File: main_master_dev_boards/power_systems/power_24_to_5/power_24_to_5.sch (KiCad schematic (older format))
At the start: 31 parts, among them J1 Switch_in, J2 24_in, J3 GND_in, J4 PGoodMain_out, J5 ref_out, J6 5_out, J7 GND_out, J8 3v3_out, J9 PGoodBackup_out, U1 LMR16030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

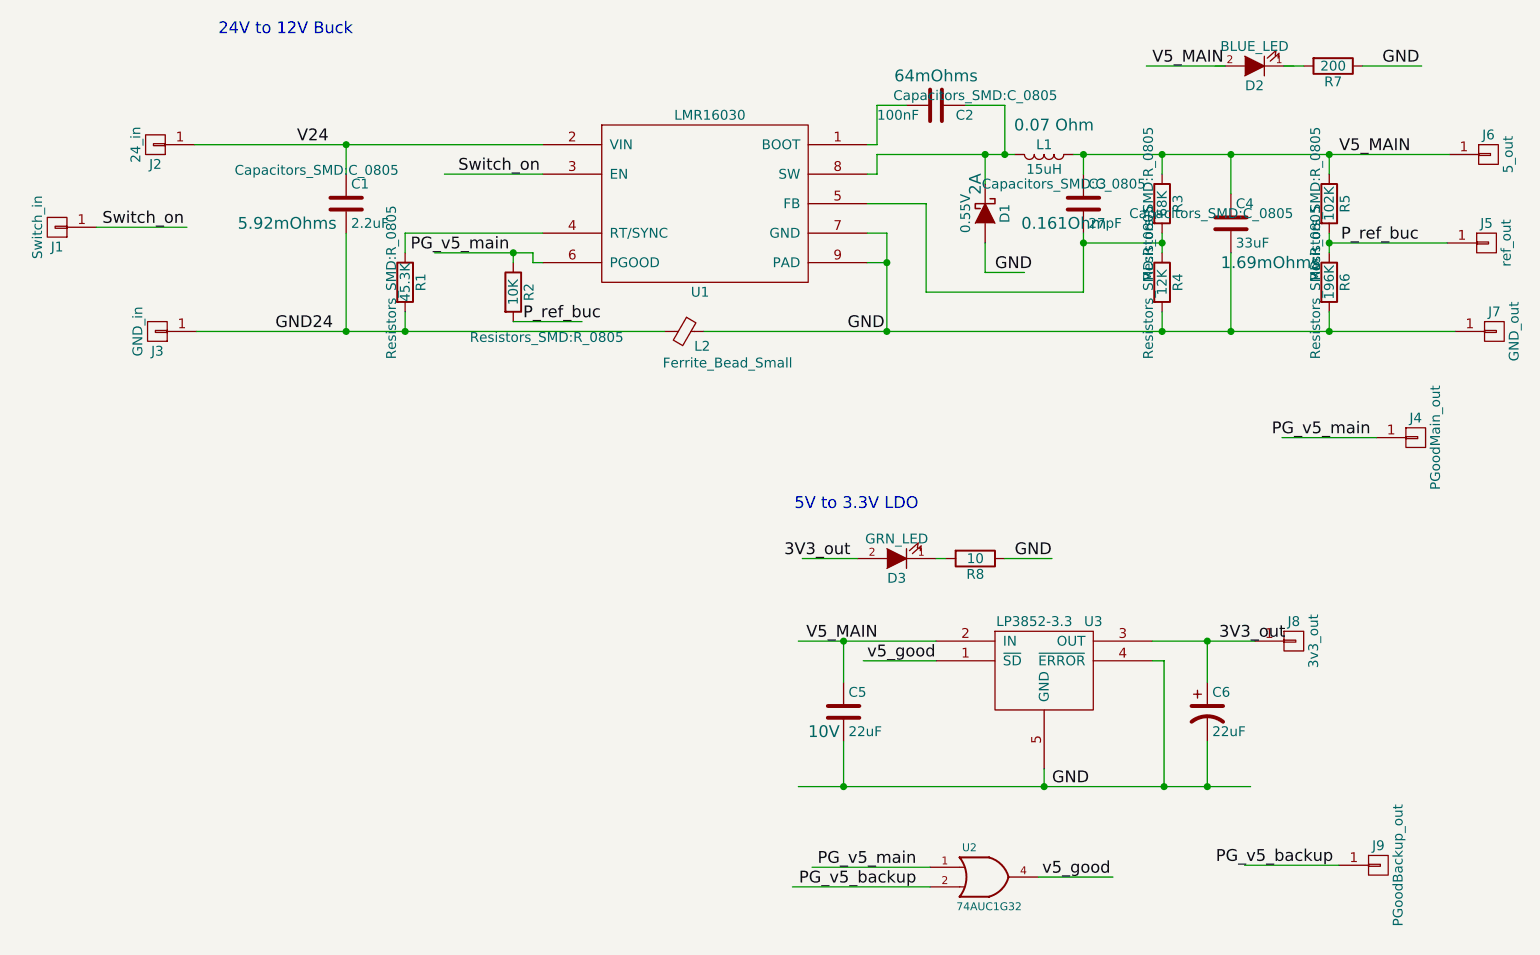
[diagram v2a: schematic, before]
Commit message: Redesigned 24 to 5 dev board
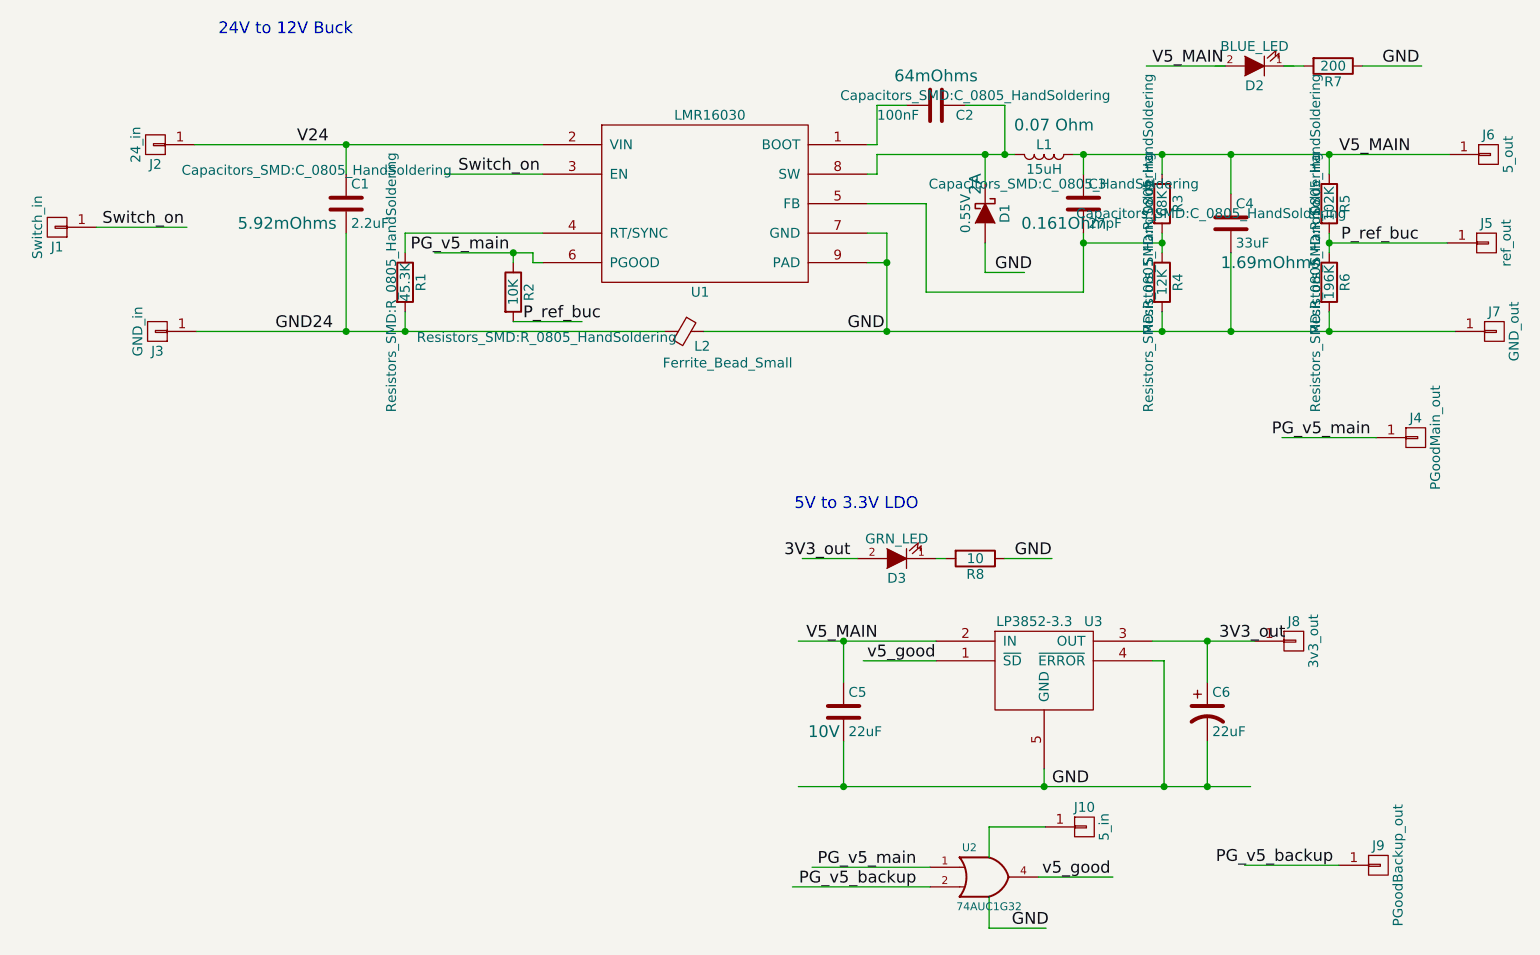
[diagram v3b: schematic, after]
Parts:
- added J10: 5_in, pinheaders:pinhead-01x01_3x1, symbol CONN_01X01
- C1, C2, C3, C4: footprint Capacitors_SMD:C_0805 -> Capacitors_SMD:C_0805_HandSoldering
- C5, C6: footprint Capacitors_SMD:C_0603 -> Capacitors_SMD:C_0805_HandSoldering
- J1, J2, J4, J5, J6, J8, J9: footprint Pin_Headers:Pin_Header_Straight_1x01_Pitch2.54mm -> pinheaders:pinhead-01x01_3x1
- J3, J7: footprint Pin_Headers:Pin_Header_Straight_1x01_Pitch2.54mm -> pinheaders:pinhead-01x01_3x1_square
- L2: footprint Capacitors_SMD:C_0603_HandSoldering -> Capacitors_SMD:C_0805_HandSoldering
- R1, R2, R3, R4, R5, R6, R7: footprint Resistors_SMD:R_0805 -> Resistors_SMD:R_0805_HandSoldering
- R8: footprint Resistors_SMD:R_0603 -> Resistors_SMD:R_0805_HandSoldering
- U1: footprint HSOIC-8:HSOIC-8-1EP_Pitch1.27mm -> HSOIC-8:HSOIC-8-1EP_Pitch1.27mm_noVias
- U2: footprint SO-70:SO-70 -> TO_SOT_Packages_SMD:SOT-23-5_HandSoldering
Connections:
- wire segments 67 -> 71
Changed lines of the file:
@@
 LIBS:contrib
 LIBS:valves
+LIBS:antenna
+LIBS:AS1360
+LIBS:conn_2x45
+LIBS:conn_2x50
+LIBS:conn_open_q_x2
+LIBS:esd7c5
+LIBS:FDS4935A
+LIBS:FPF1203LUCX
+LIBS:lan9512
+LIBS:LMR16020
+LIBS:LP3852-3.3
+LIBS:LTC2955-1
+LIBS:MIC2026
+LIBS:Si1077X
+LIBS:Si1900DL
+LIBS:SN74LV1T125
+LIBS:SN74LV4T125
+LIBS:TDP6E001RSER
+LIBS:tps82084sil
+LIBS:TPS754
+LIBS:TPS61089
+LIBS:TPS61232DRC
+LIBS:TPS832130SIL
+LIBS:0s102011ma1qn1
+LIBS:74LVC1G17
+LIBS:74V1T126
+LIBS:acs711klctr-12ab-t
+LIBS:AD7192
+LIBS:AD7193
+LIBS:am-hrr30-xxx
+LIBS:aon7528
+LIBS:AP7363
+LIBS:AS1359
+LIBS:csd16323q3
+LIBS:dmn2004dmk
+LIBS:dp_devices
+LIBS:DSPIC33E128MC506
+LIBS:fds6898az
+LIBS:ina197
+LIBS:irf7329pbf
+LIBS:ld1117
+LIBS:lm3478
+LIBS:lm3481
+LIBS:lt1910
+LIBS:ltc1871
+LIBS:ltc1982
+LIBS:MAG3110
+LIBS:mcp1700
+LIBS:mcp73831
+LIBS:mcsmt-g5030a1-3712
+LIBS:microchip_can
+LIBS:microclasp_hdrx2
+LIBS:microclasp_hdrx3
+LIBS:MPU-6000_MPU-6050
+LIBS:MPU-9150
+LIBS:nrf24l01+
+LIBS:pds1040l
+LIBS:pic12f1571
+LIBS:pinhead
+LIBS:psmn013-80ys
+LIBS:RESISTOR_ARRAY
+LIBS:rf803d
+LIBS:RGB_LED
+LIBS:Si1970DH
+LIBS:sn65hvd232
+LIBS:ssc54
+LIBS:sw_push_4
+LIBS:tc74
+LIBS:tps54540
+LIBS:TPS2113A
+LIBS:vs-mbrb1635pbf
+LIBS:xal5050-562meb
+LIBS:xal6030-182mec
+LIBS:ld29150dt50r
+LIBS:ncp59151ds50r4g
+LIBS:pinhd-2x23
 LIBS:main_master_board-cache
 LIBS:power_24_to_5-cache
@@
 F 0 "C3" H 6075 2700 50  0000 L CNN
 F 1 "27pF" H 6075 2500 50  0000 L CNN
-F 2 "Capacitors_SMD:C_0805" H 5950 2700 50  0000 C CNN
+F 2 "Capacitors_SMD:C_0805_HandSoldering" H 5950 2700 50  0000 C CNN
 F 3 "" H 6050 2600 50  0000 C CNN
 F 4 "0.161Ohm" H 5950 2500 60  0000 C CNN "Resistance"
@@
 F 0 "C1" H 2325 2700 50  0000 L CNN
 F 1 "2.2uF" H 2325 2500 50  0000 L CNN
-F 2 "Capacitors_SMD:C_0805" H 2150 2770 50  0000 C CNN
+F 2 "Capacitors_SMD:C_0805_HandSoldering" H 2150 2770 50  0000 C CNN
 F 3 "" H 2300 2600 50  0001 C CNN
 F 4 "5.92mOhms" H 2000 2500 60  0000 C CNN "Resistance"
@@
 F 0 "R1" V 2680 3000 50  0000 C CNN
 F 1 "45.3K" V 2600 3000 50  0000 C CNN
-F 2 "Resistors_SMD:R_0805" V 2530 3000 50  0000 C CNN
+F 2 "Resistors_SMD:R_0805_HandSoldering" V 2530 3000 50  0000 C CNN
 F 3 "" H 2600 3000 50  0000 C CNN
 F 4 "d" V 2600 3000 60  0001 C CNN "Field4"
@@
 F 0 "C2" V 5350 2200 50  0000 L CNN
 F 1 "100nF" V 5350 1800 50  0000 L CNN
-F 2 "Capacitors_SMD:C_0805" V 5250 2300 50  0000 C CNN
+F 2 "Capacitors_SMD:C_0805_HandSoldering" V 5250 2300 50  0000 C CNN
 F 3 "https://product.tdk.com/info/en/catalog/datasheets/mlcc%5Fcommercial%5Fgeneral%5Fen.pdf" H 5300 2100 50  0001 C CNN
 F 4 "64mOhms" V 5150 2100 60  0000 C CNN "Resistance"
@@
 F 0 "R3" V 6530 2600 50  0000 C CNN
 F 1 "68K" V 6450 2600 50  0000 C CNN
-F 2 "Resistors_SMD:R_0805" V 6380 2600 50  0000 C CNN
+F 2 "Resistors_SMD:R_0805_HandSoldering" V 6380 2600 50  0000 C CNN
 F 3 "" H 6450 2600 50  0000 C CNN
 F 4 "d" V 6450 2600 60  0001 C CNN "Field4"
@@
 F 0 "R4" V 6530 3000 50  0000 C CNN
 F 1 "12K" V 6450 3000 50  0000 C CNN
-F 2 "Resistors_SMD:R_0805" V 6380 3000 50  0000 C CNN
+F 2 "Resistors_SMD:R_0805_HandSoldering" V 6380 3000 50  0000 C CNN
 F 3 "" H 6450 3000 50  0000 C CNN
 F 4 "d" V 6450 3000 60  0001 C CNN "Field4"
@@
 F 0 "C4" H 6825 2800 50  0000 L CNN
 F 1 "33uF" H 6825 2600 50  0000 L CNN
-F 2 "Capacitors_SMD:C_0805" H 6700 2750 50  0000 C CNN
+F 2 "Capacitors_SMD:C_0805_HandSoldering" H 6700 2750 50  0000 C CNN
 F 3 "" H 6800 2700 50  0000 C CNN
 F 4 "1.69mOhms" H 7000 2500 60  0000 C CNN "Resistance"
@@
 F 0 "R2" V 3230 3050 50  0000 C CNN
 F 1 "10K" V 3150 3050 50  0000 C CNN
-F 2 "Resistors_SMD:R_0805" H 3320 2820 50  0000 C CNN
+F 2 "Resistors_SMD:R_0805_HandSoldering" H 3320 2820 50  0000 C CNN
 F 3 "" H 3150 3050 50  0000 C CNN
 	1    3150 3050
@@
 F 0 "R7" V 7400 1900 50  0000 C CNN
 F 1 "200" V 7320 1900 50  0000 C CNN
-F 2 "Resistors_SMD:R_0805" V 7250 1900 50  0001 C CNN
+F 2 "Resistors_SMD:R_0805_HandSoldering" V 7250 1900 50  0001 C CNN
 F 3 "" H 7320 1900 50  0000 C CNN
 	1    7320 1900
@@
 F 0 "U1" H 4100 2150 50  0000 C CNN
 F 1 "LMR16030" H 4150 3050 50  0000 C CNN
-F 2 "HSOIC-8:HSOIC-8-1EP_Pitch1.27mm" H 3750 2150 50  0001 C CNN
+F 2 "HSOIC-8:HSOIC-8-1EP_Pitch1.27mm_noVias" H 3750 2150 50  0001 C CNN
 F 3 "http://www.digikey.com/product-detail/en/LMR16030PDDA/296-44513-5-ND/" H 4550 2150 50  0001 C CNN
 	1    4150 2600
@@
 F 0 "R5" V 7380 2600 50  0000 C CNN
 F 1 "102K" V 7300 2600 50  0000 C CNN
-F 2 "Resistors_SMD:R_0805" V 7230 2600 50  0000 C CNN
+F 2 "Resistors_SMD:R_0805_HandSoldering" V 7230 2600 50  0000 C CNN
 F 3 "" H 7300 2600 50  0000 C CNN
 	1    7300 2600
@@
 F 0 "R6" V 7380 3000 50  0000 C CNN
 F 1 "196K" V 7300 3000 50  0000 C CNN
-F 2 "Resistors_SMD:R_0805" V 7230 3000 50  0000 C CNN
+F 2 "Resistors_SMD:R_0805_HandSoldering" V 7230 3000 50  0000 C CNN
 F 3 "" H 7300 3000 50  0000 C CNN
 	1    7300 3000
@@
 F 0 "J2" H 1330 2400 50  0000 C CNN
 F 1 "24_in" V 1430 2300 50  0000 C CNN
-F 2 "Pin_Headers:Pin_Header_Straight_1x01_Pitch2.54mm" H 1330 2300 50  0001 C CNN
+F 2 "pinheaders:pinhead-01x01_3x1" H 1330 2300 50  0001 C CNN
 F 3 "" H 1330 2300 50  0001 C CNN
 	1    1330 2300
@@
 F 0 "J3" H 1340 3350 50  0000 C CNN
 F 1 "GND_in" V 1440 3250 50  0000 C CNN
-F 2 "Pin_Headers:Pin_Header_Straight_1x01_Pitch2.54mm" H 1340 3250 50  0001 C CNN
+F 2 "pinheaders:pinhead-01x01_3x1_square" H 1340 3250 50  0001 C CNN
 F 3 "" H 1340 3250 50  0001 C CNN
 	1    1340 3250
@@
 F 0 "J4" H 7740 3890 50  0000 C CNN
 F 1 "PGoodMain_out" V 7840 3790 50  0000 C CNN
-F 2 "Pin_Headers:Pin_Header_Straight_1x01_Pitch2.54mm" H 7740 3790 50  0001 C CNN
+F 2 "pinheaders:pinhead-01x01_3x1" H 7740 3790 50  0001 C CNN
 F 3 "" H 7740 3790 50  0001 C CNN
 	1    7740 3790
@@
 F 0 "J6" H 8110 2450 50  0000 C CNN
 F 1 "5_out" V 8210 2350 50  0000 C CNN
-F 2 "Pin_Headers:Pin_Header_Straight_1x01_Pitch2.54mm" H 8110 2350 50  0001 C CNN
+F 2 "pinheaders:pinhead-01x01_3x1" H 8110 2350 50  0001 C CNN
 F 3 "" H 8110 2350 50  0001 C CNN
 	1    8110 2350
@@
 F 0 "J7" H 8140 3350 50  0000 C CNN
 F 1 "GND_out" V 8240 3250 50  0000 C CNN
-F 2 "Pin_Headers:Pin_Header_Straight_1x01_Pitch2.54mm" H 8140 3250 50  0001 C CNN
+F 2 "pinheaders:pinhead-01x01_3x1_square" H 8140 3250 50  0001 C CNN
 F 3 "" H 8140 3250 50  0001 C CNN
 	1    8140 3250
@@
 F 0 "J5" H 8100 2900 50  0000 C CNN
 F 1 "ref_out" V 8200 2800 50  0000 C CNN
-F 2 "Pin_Headers:Pin_Header_Straight_1x01_Pitch2.54mm" H 8100 2800 50  0001 C CNN
+F 2 "pinheaders:pinhead-01x01_3x1" H 8100 2800 50  0001 C CNN
 F 3 "" H 8100 2800 50  0001 C CNN
 	1    8100 2800
@@
 F 0 "J1" H 830 2820 50  0000 C CNN
 F 1 "Switch_in" V 930 2720 50  0000 C CNN
-F 2 "Pin_Headers:Pin_Header_Straight_1x01_Pitch2.54mm" H 830 2720 50  0001 C CNN
+F 2 "pinheaders:pinhead-01x01_3x1" H 830 2720 50  0001 C CNN
 F 3 "" H 830 2720 50  0001 C CNN
 	1    830  2720
@@
 F 0 "L2" V 4095 3300 50  0000 L CNN
 F 1 "Ferrite_Bead_Small" V 4180 3140 50  0000 L CNN
-F 2 "Capacitors_SMD:C_0603_HandSoldering" V 3950 3250 50  0001 C CNN
+F 2 "Capacitors_SMD:C_0805_HandSoldering" V 3950 3250 50  0001 C CNN
 F 3 "https://www.digikey.com/product-detail/en/BLM18PG121SN1D/490-1037-1-ND/" H 4020 3250 50  0001 C CNN
 	1    4020 3250
@@
 F 0 "R8" V 5580 4405 50  0000 C CNN
 F 1 "10" V 5500 4405 50  0000 C CNN
-F 2 "Resistors_SMD:R_0603" V 5430 4405 50  0001 C CNN
+F 2 "Resistors_SMD:R_0805_HandSoldering" V 5430 4405 50  0001 C CNN
 F 3 "" H 5500 4405 50  0000 C CNN
 	1    5500 4405
@@
 F 0 "C5" H 4855 5285 50  0000 L CNN
 F 1 "22uF" H 4855 5085 50  0000 L CNN
-F 2 "Capacitors_SMD:C_0603" H 4868 5035 50  0001 C CNN
+F 2 "Capacitors_SMD:C_0805_HandSoldering" H 4868 5035 50  0001 C CNN
 F 3 "" H 4830 5185 50  0000 C CNN
 F 4 "10V" H 4730 5085 60  0000 C CNN "Voltage"
@@
 F 0 "C6" H 6705 5285 50  0000 L CNN
 F 1 "22uF" H 6705 5085 50  0000 L CNN
-F 2 "Capacitors_SMD:C_0603" H 6680 5185 50  0001 C CNN
+F 2 "Capacitors_SMD:C_0805_HandSoldering" H 6680 5185 50  0001 C CNN
 F 3 "" H 6680 5185 50  0000 C CNN
 	1    6680 5185
@@
 F 0 "U2" H 5470 6175 40  0000 C CNN
 F 1 "74AUC1G32" H 5570 5875 40  0000 C CNN
-F 2 "SO-70:SO-70" H 5570 6025 60  0001 C CNN
+F 2 "TO_SOT_Packages_SMD:SOT-23-5_HandSoldering" H 5570 6025 60  0001 C CNN
 F 3 "https://octopart.com/sn74auc1g32dckr-texas+instruments-464483" H 5570 6025 60  0001 C CNN
 	1    5570 6025
@@
 F 0 "J9" H 7550 6065 50  0000 C CNN
 F 1 "PGoodBackup_out" V 7650 5965 50  0000 C CNN
-F 2 "Pin_Headers:Pin_Header_Straight_1x01_Pitch2.54mm" H 7550 5965 50  0001 C CNN
+F 2 "pinheaders:pinhead-01x01_3x1" H 7550 5965 50  0001 C CNN
 F 3 "" H 7550 5965 50  0001 C CNN
 	1    7550 5965
@@
 F 0 "J8" H 7120 4925 50  0000 C CNN
 F 1 "3v3_out" V 7220 4825 50  0000 C CNN
-F 2 "Pin_Headers:Pin_Header_Straight_1x01_Pitch2.54mm" H 7120 4825 50  0001 C CNN
+F 2 "pinheaders:pinhead-01x01_3x1" H 7120 4825 50  0001 C CNN
 F 3 "" H 7120 4825 50  0001 C CNN
 	1    7120 4825
@@
 Text Label 4865 4405 2    60   ~ 0
 3V3_out
+Wire Wire Line
+	5570 5925 5570 5770
+Wire Wire Line
+	5570 5770 5855 5770
+Wire Wire Line
+	5570 6125 5570 6285
+Wire Wire Line
+	5570 6285 5860 6285
+Text Label 5685 6285 0    60   ~ 0
+GND
+$Comp
+L CONN_01X01 J10
+U 1 1 592615A0
+P 6055 5770
+F 0 "J10" H 6055 5870 50  0000 C CNN
+F 1 "5_in" V 6155 5770 50  0000 C CNN
+F 2 "pinheaders:pinhead-01x01_3x1" H 6055 5770 50  0001 C CNN
+F 3 "" H 6055 5770 50  0001 C CNN
+	1    6055 5770
+	1    0    0    -1
+$EndComp
 $EndSCHEMATC

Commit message: Created new branch and modified 24 to 5 buck with values from datasheet
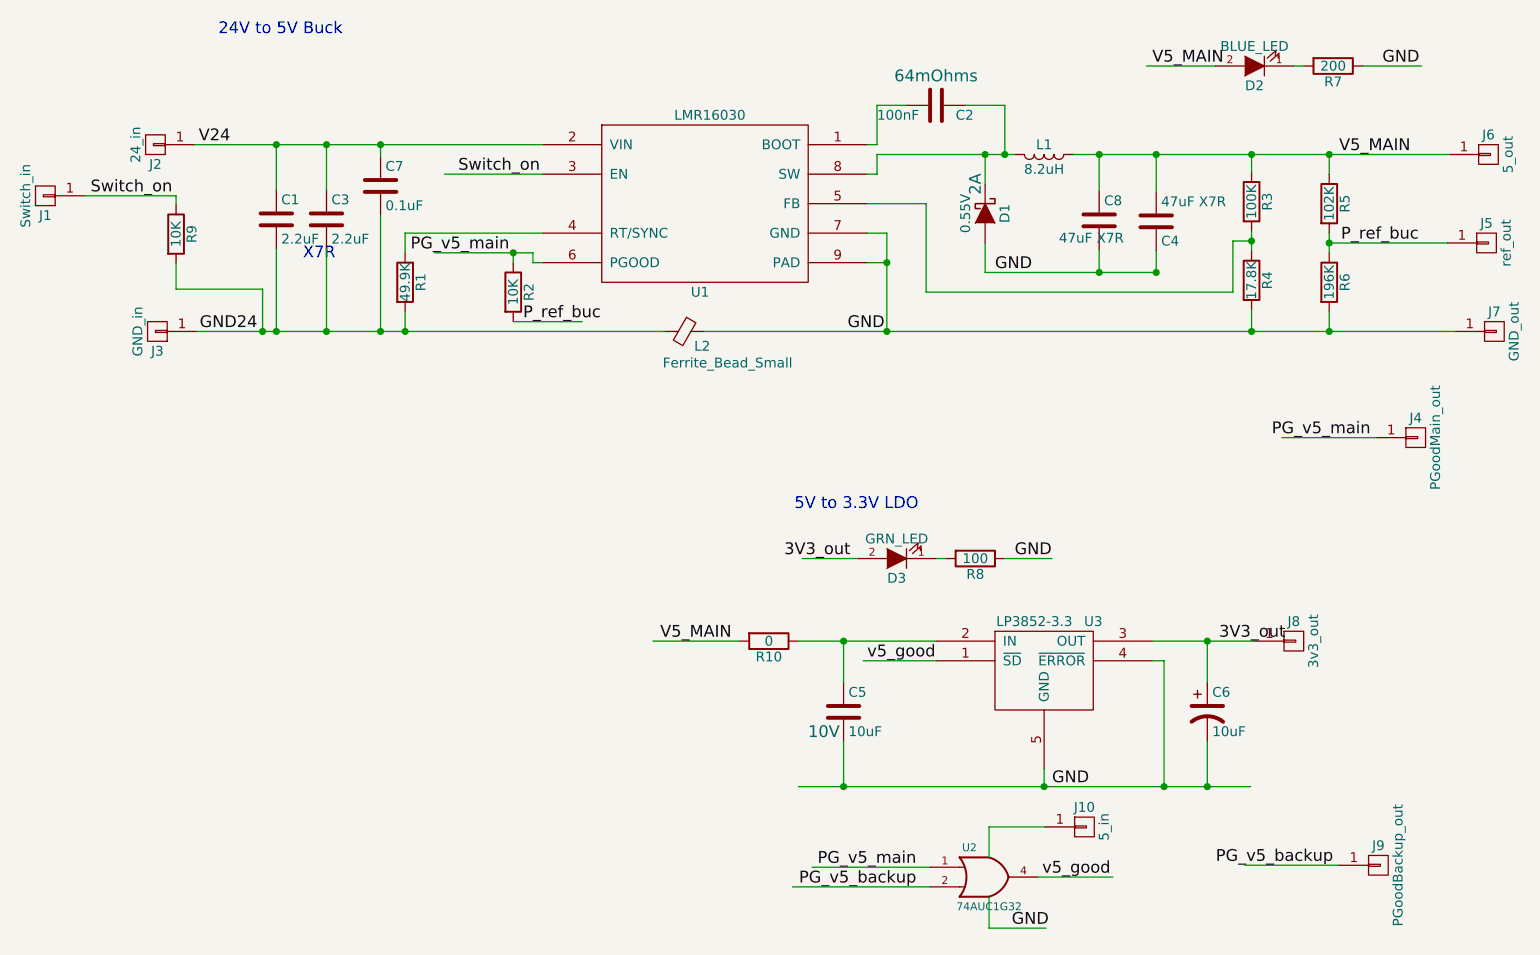
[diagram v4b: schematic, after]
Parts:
- added C7: 0.1uF, Capacitors_SMD:C_0805_HandSoldering, symbol C
- added C8: 47uF X7R, Capacitors_SMD:C_0805_HandSoldering, symbol C
- added R10: 0, Resistors_SMD:R_0603, symbol R
- added R9: 10K, Resistors_SMD:R_0805_HandSoldering, symbol R
- C3: value 27pF -> 2.2uF; Field5 C0805C270J5GACTU -> C1005X5R1V225K050BC; Resistance 0.161Ohm -> 5.92mOhms
- C4: value 33uF -> 47uF X7R
- C5, C6: value 22uF -> 10uF
- L1: value 15uH -> 8.2uH; footprint Bourns:Bourns-8040 -> Bourns:Bourns-SRP7028A; Field5 SRN8040-150M -> (none); Resistance 0.07 Ohm -> (none)
- R1: value 45.3K -> 49.9K
- R3: value 68K -> 100K
- R4: value 12K -> 17.8K
- R8: value 10 -> 100
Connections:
- wire segments 71 -> 81
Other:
- note added: "24V to 5V Buck"
- note added: "X7R"
- note removed: "24V to 12V Buck"
- moved on the sheet: C1, C4, J1, R3, R4
